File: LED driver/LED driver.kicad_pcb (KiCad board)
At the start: 2 copper layers, 78.5 x 59 mm, 45 parts, among them J1 Conn_VCC, J2 Conn_LED, J3 Conn_UART, J4 Conn_ESP32, P1 USB_C_Receptacle_USB2.0, Q1 IRFZ44NS, Q2 IRFZ44NS, Q3 IRFZ44NS, Q4 IRFZ44NS, Q5 IRFZ44NS, SW1 SW_Push, U1 ESP32-S2-WROVER-I, U2 MP2359

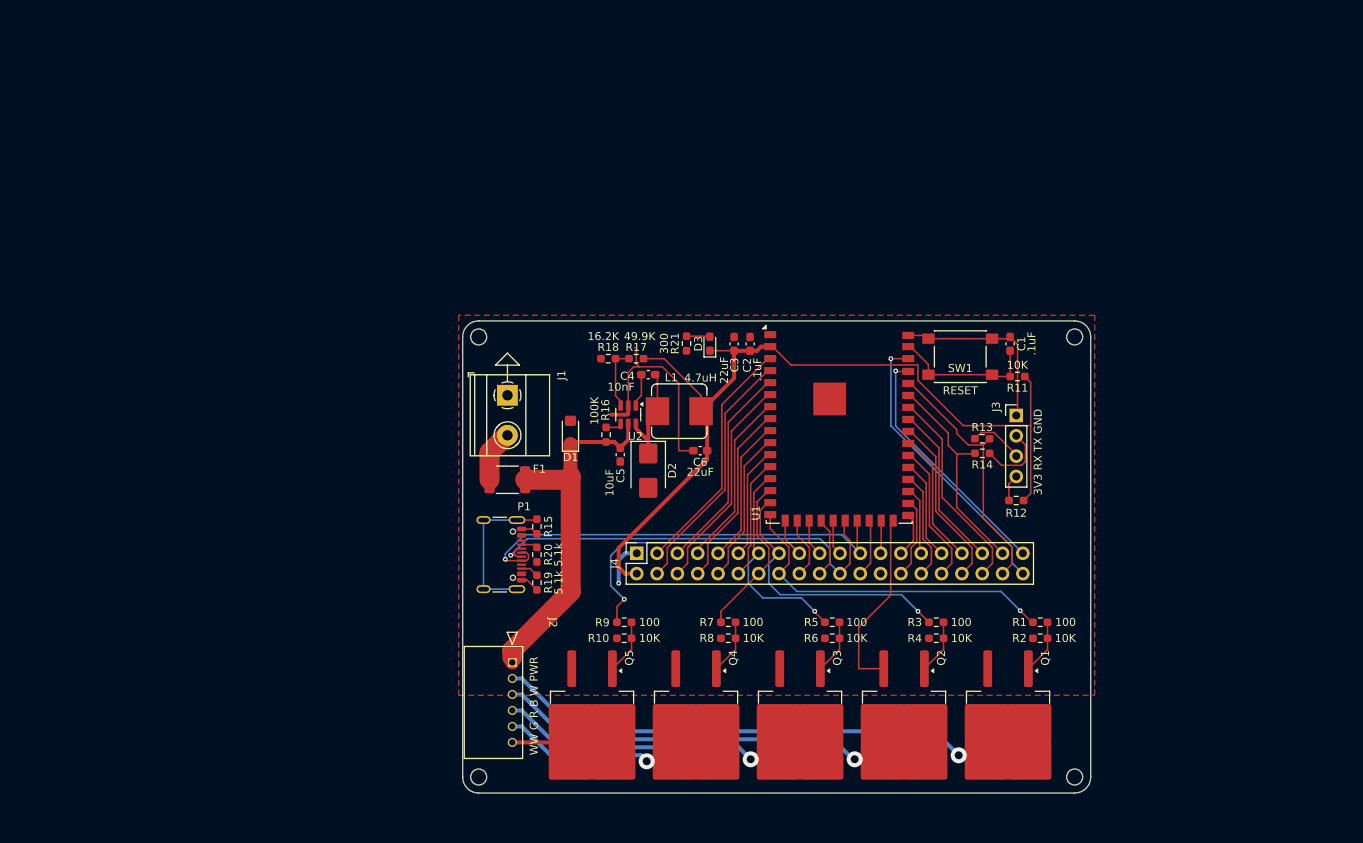
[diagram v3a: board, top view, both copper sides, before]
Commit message: work on LED driver (WIP)
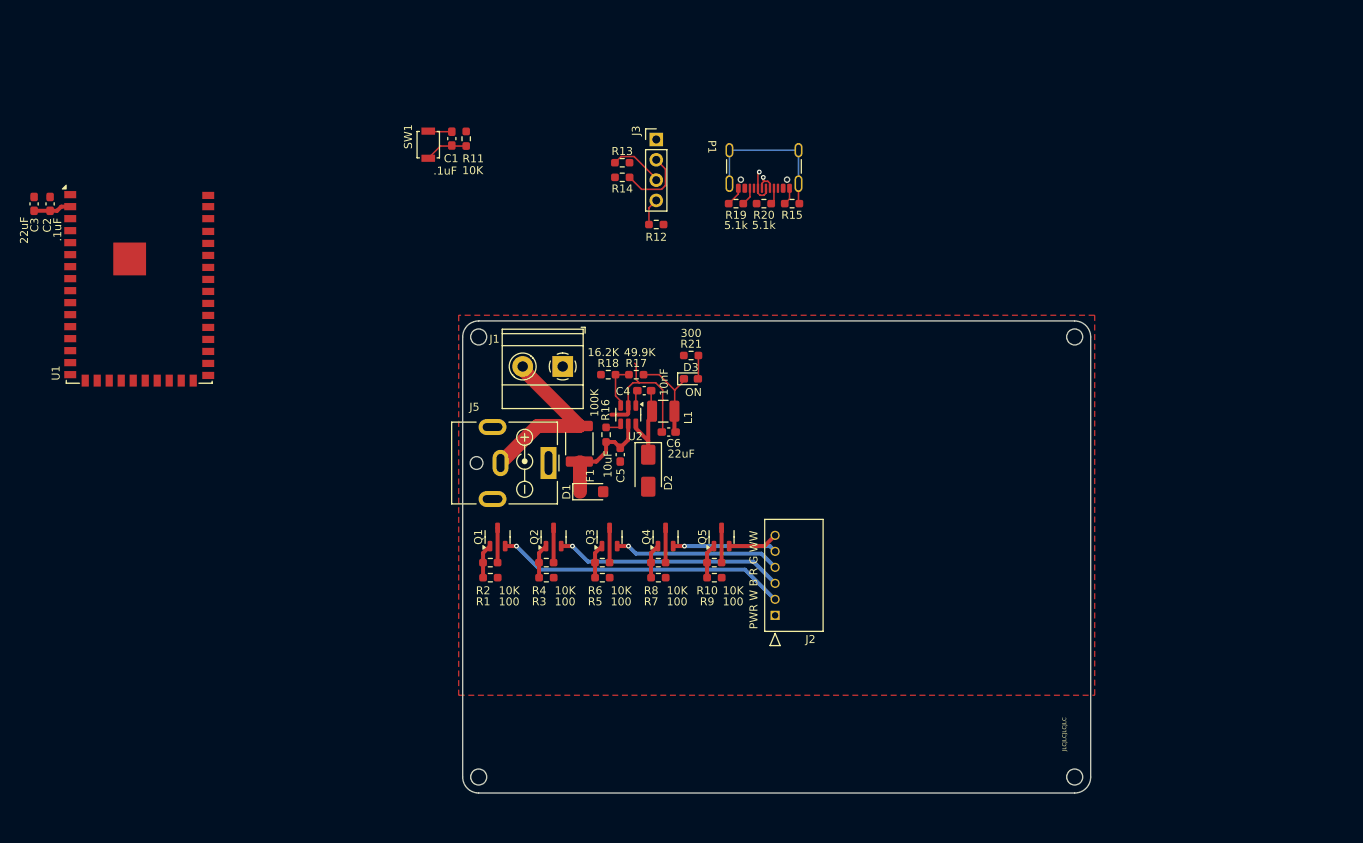
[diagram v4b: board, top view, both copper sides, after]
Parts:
- removed J4: Conn_ESP32, Connector_PinSocket_2.54mm:PinSocket_2x20_P2.54mm_Vertical
- added J5: Conn_VCC, Connector_BarrelJack:BarrelJack_CUI_PJ-063AH_Horizontal, F.Cu at (110.0, 75.0)
- D2: footprint Diode_SMD:D_SMB -> Diode_SMD:D_SMA
- J1: value Conn_VCC -> Conn_VCC_ALT
- L1: footprint Inductor_SMD:L_Bourns_SRP7028A_7.3x6.6mm -> Inductor_SMD:L_1210_3225Metric
- Q1, Q2, Q3, Q4, Q5: footprint Package_TO_SOT_SMD:TO-263-2 -> Package_TO_SOT_SMD:SOT-23-3
- SW1: footprint Button_Switch_SMD:SW_Push_1P1T_NO_6x6mm_H9.5mm -> Button_Switch_SMD:SW_SPST_B3U-1000P
- moved C2 89.2 mm to (47.7, 42.6)
- moved C3 89.2 mm to (45.7, 42.6)
- moved U1 89.2 mm to (58.9, 53.3)
- moved R11 75.0 mm to (99.7, 34.5), turned to -90 degrees
- moved C1 74.4 mm to (97.9, 34.5)
- moved SW1 71.6 mm to (95.0, 35.2), turned to -90 degrees
- moved R2 69.4 mm to (102.8, 87.5), turned to 0 degrees
- moved R1 69.0 mm to (102.8, 89.4), turned to 0 degrees
- moved Q1 68.2 mm to (103.7, 84.3), turned to 90 degrees
- moved P1 60.0 mm to (137.0, 37.0), turned to 180 degrees
- moved R12 56.7 mm to (123.5, 45.2)
- moved R13 56.7 mm to (119.2, 37.5)
- moved J3 56.7 mm to (123.5, 34.6)
- moved R14 56.7 mm to (119.3, 39.3)
- moved R19 53.5 mm to (133.5, 42.6), turned to 180 degrees
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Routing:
- net +3.3V: track 109.0 -> 16.4 mm
- net /22: track 55.4 -> 2.96 mm
- net /23: track 55.8 -> 4.60 mm
- net /16: track 43.1 -> 0.00 mm, vias 1 -> 0
- net /17: track 39.0 -> 0.00 mm, vias 1 -> 0
- net GND: track 84.8 -> 47.3 mm, vias 1 -> 0
- net /40: track 35.9 -> 0.00 mm, vias 1 -> 0
- net /15: track 34.3 -> 0.00 mm, vias 1 -> 0
- net +24V: track 45.8 -> 13.7 mm
- net /38: track 32.0 -> 0.00 mm
- net /4: track 31.4 -> 0.00 mm
- net /39: track 31.0 -> 0.00 mm, vias 1 -> 0
- net /3: track 30.4 -> 0.00 mm
- net /6: track 27.4 -> 0.00 mm
- net /37: track 27.1 -> 0.00 mm
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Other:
- board text added: "JLCJLCJLCJLC"
- board text added: "ON"
- board text added: "PWR W B R G WW"
- board text removed: "3V3 RX TX GND"
- board text removed: "RESET"
- board text removed: "WW G R B W PWR"

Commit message: mostly finish led driver
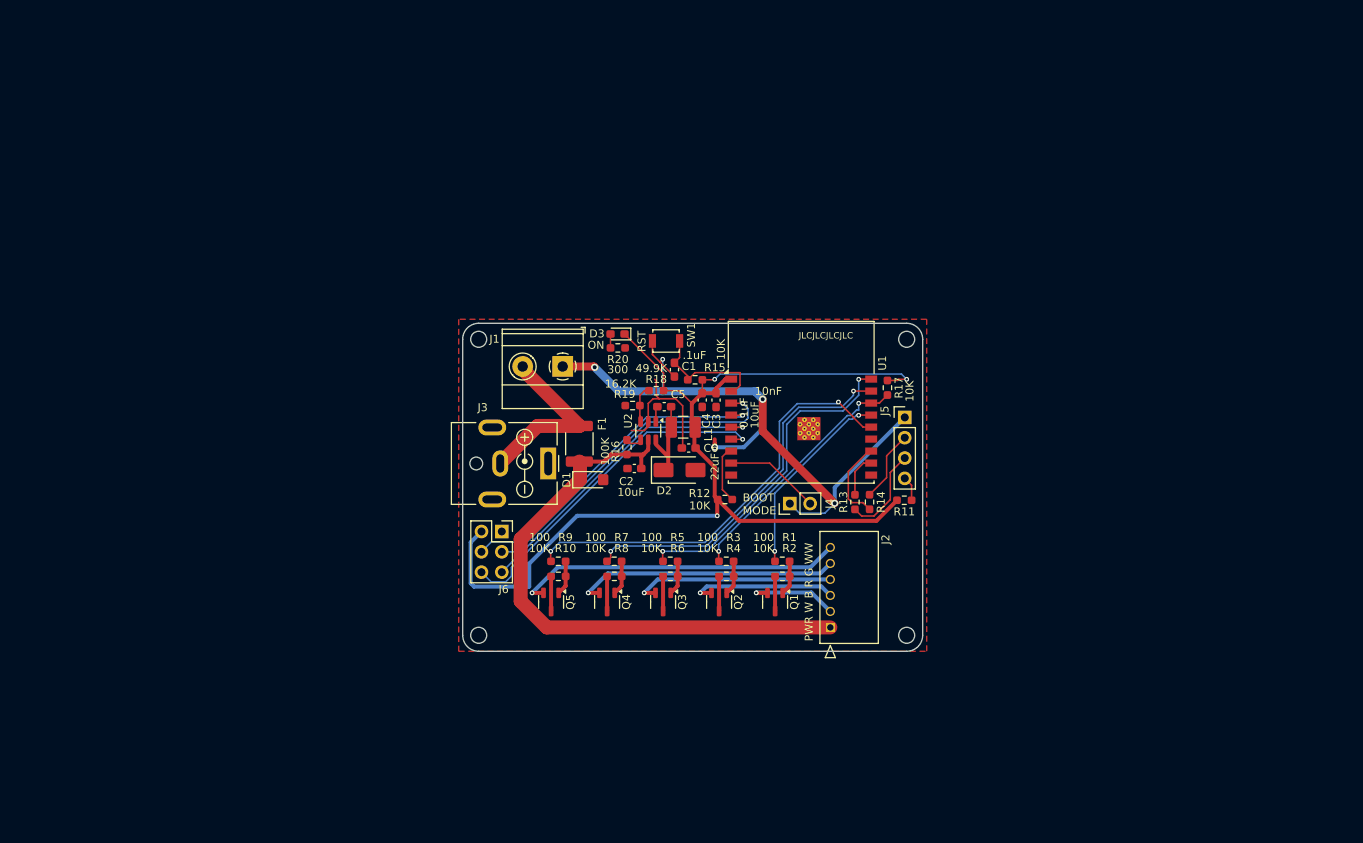
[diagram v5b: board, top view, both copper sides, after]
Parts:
- removed P1: USB_C_Receptacle_USB2.0, Connector_USB:USB_C_Receptacle_GCT_USB4105-xx-A_16P_TopMnt_Horizontal
- removed R21: 300, Custom:R_0603_HandSolder_ValuePrinted
- added J4: Conn_Boot_Mode, Connector_PinHeader_2.54mm:PinHeader_1x02_P2.54mm_Vertical, F.Cu at (140.2, 80.1)
- added J6: Conn_Aux, Connector_PinSocket_2.54mm:PinSocket_2x03_P2.54mm_Vertical, F.Cu at (104.2, 83.6)
- C2: value .1uF -> 10uF
- C3: value 22uF -> 10uF
- C4: value 10nF -> 0.1uF
- C5: value 10uF -> 10nF
- J3: value Conn_UART -> Conn_VCC; footprint Connector_PinHeader_2.54mm:PinHeader_1x04_P2.54mm_Vertical -> Connector_BarrelJack:BarrelJack_CUI_PJ-063AH_Horizontal
- J5: value Conn_VCC -> Conn_UART; footprint Connector_BarrelJack:BarrelJack_CUI_PJ-063AH_Horizontal -> Connector_PinHeader_2.54mm:PinHeader_1x04_P2.54mm_Vertical
- L1: footprint Inductor_SMD:L_1210_3225Metric -> Inductor_SMD:L_1210_3225Metric_Pad1.42x2.65mm_HandSolder
- R11: value 10K -> 0; footprint Custom:R_0603_HandSolder_ValuePrinted -> Resistor_SMD:R_0603_1608Metric_Pad0.98x0.95mm_HandSolder
- R12, R15: value 0 -> 10K; footprint Resistor_SMD:R_0603_1608Metric_Pad0.98x0.95mm_HandSolder -> Custom:R_0603_HandSolder_ValuePrinted
- R17: value 49.9K -> 10K
- R18: value 16.2K -> 49.9K
- R19: value 5.1k -> 16.2K
- R20: value 5.1k -> 300
- U1: value ESP32-S2-WROVER-I -> ESP32-C3-WROOM-02; footprint Custom:ESP32-S2-WROVER -> RF_Module:ESP32-C3-WROOM-02
- moved C3 88.7 mm to (131.0, 67.2)
- moved U1 84.5 mm to (141.6, 70.6)
- moved C2 80.2 mm to (120.8, 75.7), turned to 180 degrees
- moved R11 71.0 mm to (154.5, 79.7), turned to 180 degrees
- moved R13 51.4 mm to (148.3, 79.9), turned to 90 degrees
- moved R14 51.0 mm to (150.2, 79.9), turned to -90 degrees
- moved J5 44.9 mm to (154.6, 69.3), turned to 0 degrees
- moved J3 42.7 mm to (110.0, 75.1), turned to -90 degrees
- moved C1 40.1 mm to (125.8, 63.4), turned to 90 degrees
- moved SW1 38.5 mm to (124.7, 59.8), turned to 0 degrees
- moved R2 36.5 mm to (139.3, 89.2), turned to 180 degrees
- moved R1 36.5 mm to (139.3, 87.3), turned to 180 degrees
- moved Q1 35.6 mm to (138.4, 92.4), turned to -90 degrees
- moved R12 35.4 mm to (132.1, 79.6)
- moved R17 31.4 mm to (152.4, 65.6), turned to -90 degrees
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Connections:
- C2 pad 1: +3.3V -> +24V
- C3 pad 1: +3.3V -> GND
- C3 pad 2: GND -> +3.3V
- C4 pad 1: Net-(U2-BST) -> GND
- C4 pad 2: Net-(D2-K) -> +3.3V
- C5 pad 1: +24V -> Net-(U2-BST)
- C5 pad 2: GND -> Net-(D2-K)
- J3 pad 2: /TX -> Net-(J1-Pin_2)
- J5 pad 2: Net-(J1-Pin_2) -> /TX
- R1 pad 2: /16 -> /PWM_W
- R11 pad 1: +3.3V -> Net-(J5-Pin_4)
- R11 pad 2: Net-(U1-EN) -> +3.3V
- R12 pad 1: Net-(J3-Pin_4) -> +3.3V
- R12 pad 2: +3.3V -> Net-(U1-IO8)
- R13 pad 2: /38 -> Net-(U1-RXD)
- R14 pad 2: /37 -> Net-(U1-TXD)
- R15 pad 1: Net-(P1-SHIELD) -> +3.3V
- R15 pad 2: GND -> Net-(U1-EN)
- R17 pad 1: Net-(U2-FB) -> +3.3V
- R17 pad 2: +3.3V -> /PWM_B
- R18 pad 1: GND -> Net-(U2-FB)
- R18 pad 2: Net-(U2-FB) -> +3.3V
- R19 pad 1: Net-(P1-CC2) -> GND
- R19 pad 2: GND -> Net-(U2-FB)
- R20 pad 1: Net-(P1-CC1) -> GND
- R20 pad 2: GND -> Net-(D3-A)
- R3 pad 2: /15 -> /PWM_B
- R5 pad 2: /13 -> /PWM_R
- R7 pad 2: /14 -> /PWM_G
- R9 pad 2: /17 -> /PWM_WW
- U1 pad 1: GND -> +3.3V
- U1 pad 10: /10 -> unconnected-(U1-IO10-Pad10)
- U1 pad 11: /11 -> Net-(U1-RXD)
- U1 pad 12: /12 -> Net-(U1-TXD)
- U1 pad 13: /13 -> unconnected-(U1-IO18-Pad13)
- U1 pad 14: /14 -> /PWM_WW
- U1 pad 15: /15 -> /PWM_W
- U1 pad 16: /16 -> /PWM_B
- U1 pad 17: /17 -> /PWM_G
- U1 pad 18: /18 -> /PWM_R
- U1 pad 19: /19 -> GND
- U1 pad 2: +3.3V -> Net-(U1-EN)
- U1 pad 3: /3 -> /IO4
- U1 pad 4: /4 -> /IO5
- U1 pad 5: /5 -> /IO6
- U1 pad 6: /6 -> /IO7
- U1 pad 7: /7 -> Net-(U1-IO8)
- U1 pad 8: /8 -> Net-(J4-Pin_2)
- U1 pad 9: /9 -> GND
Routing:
- net +3.3V: track 16.4 -> 136.6 mm, vias 0 -> 3
- net GND: track 47.3 -> 125.4 mm, vias 0 -> 5
- net +24V: track 13.7 -> 72.4 mm
- net /PWM_WW: track 0.00 -> 53.8 mm, vias 0 -> 2
- net /PWM_G: track 0.00 -> 46.0 mm, vias 0 -> 2
- net /IO7: track 0.00 -> 43.3 mm, vias 0 -> 1
- net /IO4: track 0.00 -> 41.3 mm, vias 0 -> 1
- net /IO5: track 0.00 -> 41.2 mm, vias 0 -> 1
- net /PWM_R: track 0.00 -> 40.9 mm, vias 0 -> 2
- net /IO6: track 0.00 -> 39.1 mm, vias 0 -> 1
- net /WW: track 6.30 -> 41.1 mm, vias 0 -> 1
- net /PWM_B: track 0.00 -> 31.5 mm, vias 0 -> 2
- net /W: track 36.5 -> 11.7 mm
- net /PWM_W: track 0.00 -> 24.6 mm, vias 0 -> 2
- net /G: track 13.0 -> 33.2 mm
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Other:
- board size 78.5 x 59 mm -> 57.5 x 41 mm
- board text added: "BOOT MODE"
- board text added: "RST"

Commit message: led driver
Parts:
- C1: value .1uF -> 0.1uF
- Q1, Q2, Q3, Q4, Q5: value IRFZ44NS -> ZXMN3A01F; footprint Package_TO_SOT_SMD:SOT-23-3 -> Package_TO_SOT_SMD:SOT-23
- moved Q5 2.01 mm to (112.4, 92.5)
- moved R10 2.00 mm to (113.3, 89.1)
- moved R9 2.00 mm to (113.3, 87.2)
- moved Q4 1.51 mm to (118.9, 92.5)
- moved R8 1.50 mm to (119.8, 89.1)
- moved R7 1.50 mm to (119.8, 87.2)
- moved Q3 1.01 mm to (125.4, 92.5)
- moved R6 1.00 mm to (126.3, 89.1)
- moved R5 1.00 mm to (126.3, 87.2)
- moved Q2 0.51 mm to (131.9, 92.5)
- moved R4 0.51 mm to (132.8, 89.1)
- moved R3 0.51 mm to (132.8, 87.2)
- moved J2 0.09 mm to (145.3, 95.5)
- moved R2 0.09 mm to (139.3, 89.1)
- moved R1 0.09 mm to (139.3, 87.2)
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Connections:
- Q1 pad 2: /W -> GND
- Q1 pad 3: GND -> /W
- Q2 pad 2: /B -> GND
- Q2 pad 3: GND -> /B
- Q3 pad 2: /R -> GND
- Q3 pad 3: GND -> /R
- Q4 pad 2: /G -> GND
- Q4 pad 3: GND -> /G
- Q5 pad 2: /WW -> GND
- Q5 pad 3: GND -> /WW
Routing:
- net GND: track 125.4 -> 117.9 mm
- net /WW: track 41.1 -> 38.2 mm
- net /W: track 11.7 -> 9.10 mm
- net /G: track 33.2 -> 30.9 mm
- net /B: track 18.5 -> 16.2 mm
- net /PWM_WW: track 53.8 -> 51.6 mm
- net /R: track 25.4 -> 23.6 mm
- net /PWM_G: track 46.0 -> 44.7 mm
- net +24V: track 72.4 -> 71.1 mm
- net /PWM_R: track 40.9 -> 39.7 mm

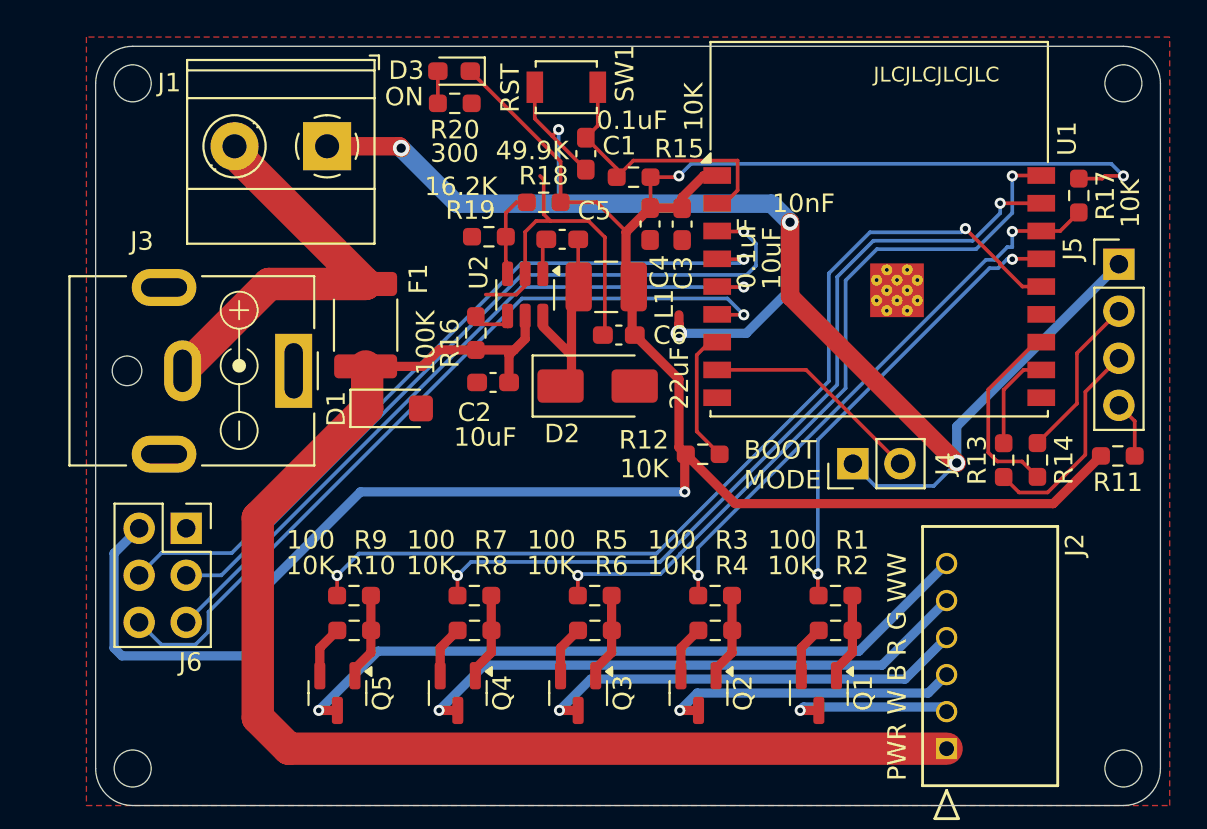
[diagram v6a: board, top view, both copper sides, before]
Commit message: led driver parts
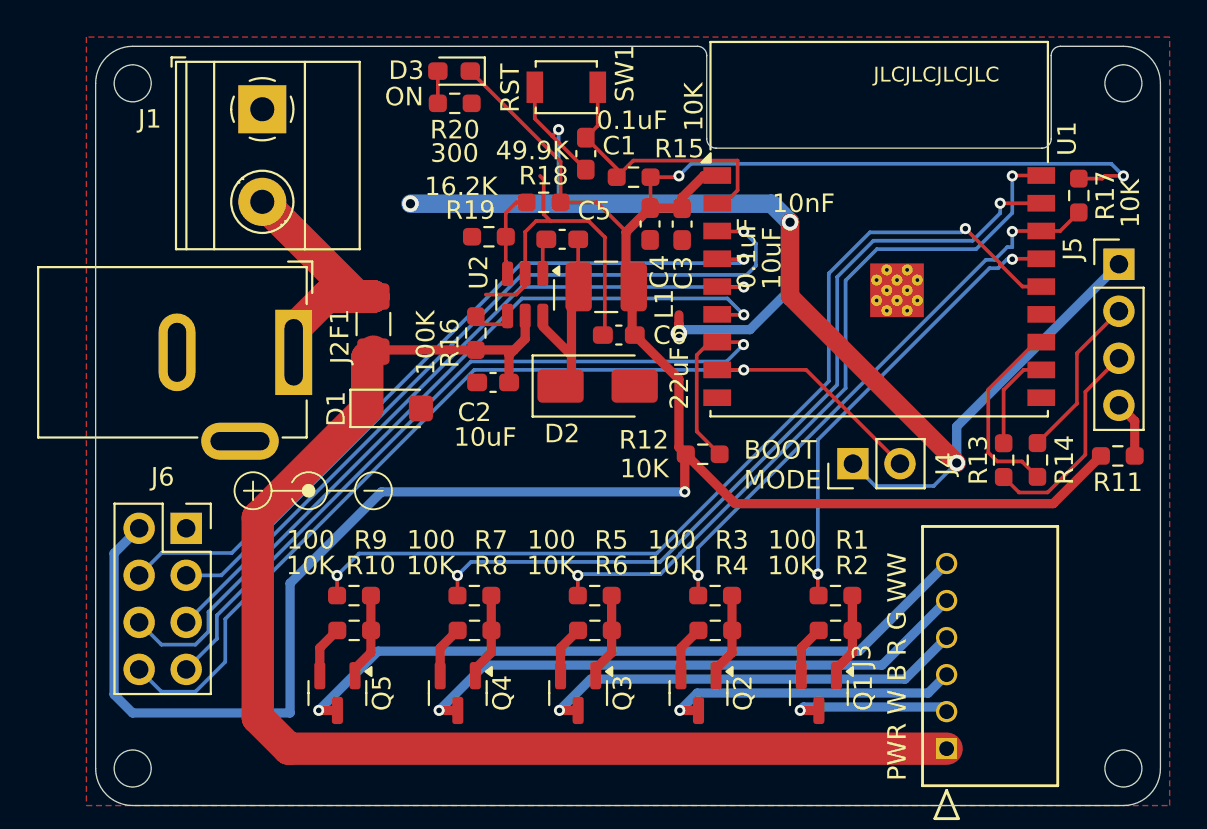
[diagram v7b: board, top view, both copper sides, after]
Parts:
- F1: value 24V 10A -> 24VDC 10A; footprint Fuse:Fuse_1812_4532Metric_Pad1.30x3.40mm_HandSolder -> Fuse:Fuse_1206_3216Metric_Pad1.42x1.75mm_HandSolder
- J1: value Conn_VCC_ALT -> Conn_VCC_Alt
- J2: renamed from J3; footprint Connector_BarrelJack:BarrelJack_CUI_PJ-063AH_Horizontal -> Connector_BarrelJack:BarrelJack_GCT_DCJ200-10-A_Horizontal
- J6: footprint Connector_PinSocket_2.54mm:PinSocket_2x03_P2.54mm_Vertical -> Connector_PinSocket_2.54mm:PinSocket_2x04_P2.54mm_Vertical
- moved J1 4.03 mm to (108.3, 61.0), turned to -90 degrees
- moved J2 1.00 mm to (110.0, 74.1)
- moved F1 0.42 mm to (114.3, 72.6)
- turned R13 to -90 degrees
- turned R14 to 90 degrees
- renumbered J2 to J3
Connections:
- net +24V renamed VCC
- J2 pad 1: GND -> Net-(J1-Pin_2)
- J2 pad 2: Net-(J1-Pin_2) -> GND
- J4 pad 2: Net-(J4-Pin_2) -> /IO9
- R12 pad 2: Net-(U1-IO8) -> /IO8
- R13 pad 1: /RX -> Net-(U1-RXD)
- R13 pad 2: Net-(U1-RXD) -> /RX
- R14 pad 1: /TX -> Net-(U1-TXD)
- R14 pad 2: Net-(U1-TXD) -> /TX
- U1 pad 7: Net-(U1-IO8) -> /IO8
- U1 pad 8: Net-(J4-Pin_2) -> /IO9
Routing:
- net /IO9: track 0.00 -> 53.7 mm, vias 0 -> 1
- net /IO8: track 0.00 -> 46.8 mm, vias 0 -> 1
- net Net-(J4-Pin_2): track 12.0 -> 0.00 mm
- net Net-(U1-IO8): track 7.26 -> 0.00 mm
- net +3.3V: track 136.6 -> 143.0 mm
- net GND: track 117.9 -> 112.1 mm
- net Net-(J1-Pin_2): track 21.8 -> 16.9 mm
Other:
- outline, holes or cut-outs redrawn
